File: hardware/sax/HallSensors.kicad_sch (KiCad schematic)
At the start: 2 parts, among them J1301 2x05_Horizontal

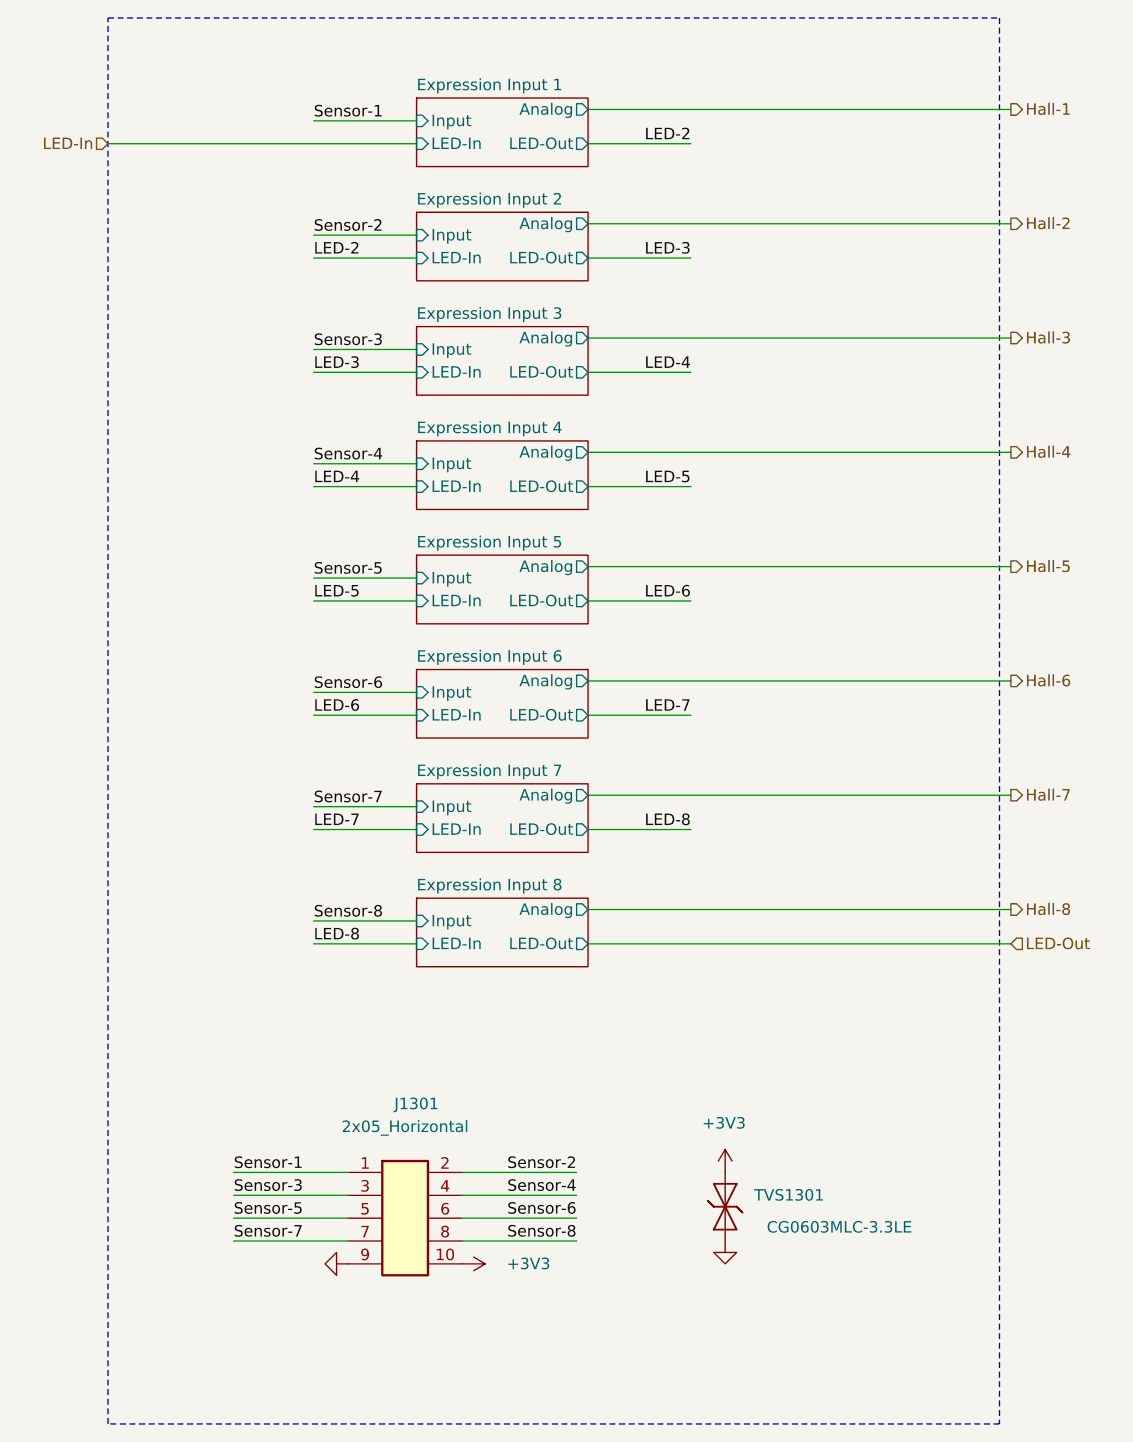
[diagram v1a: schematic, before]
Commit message: KiCad 10
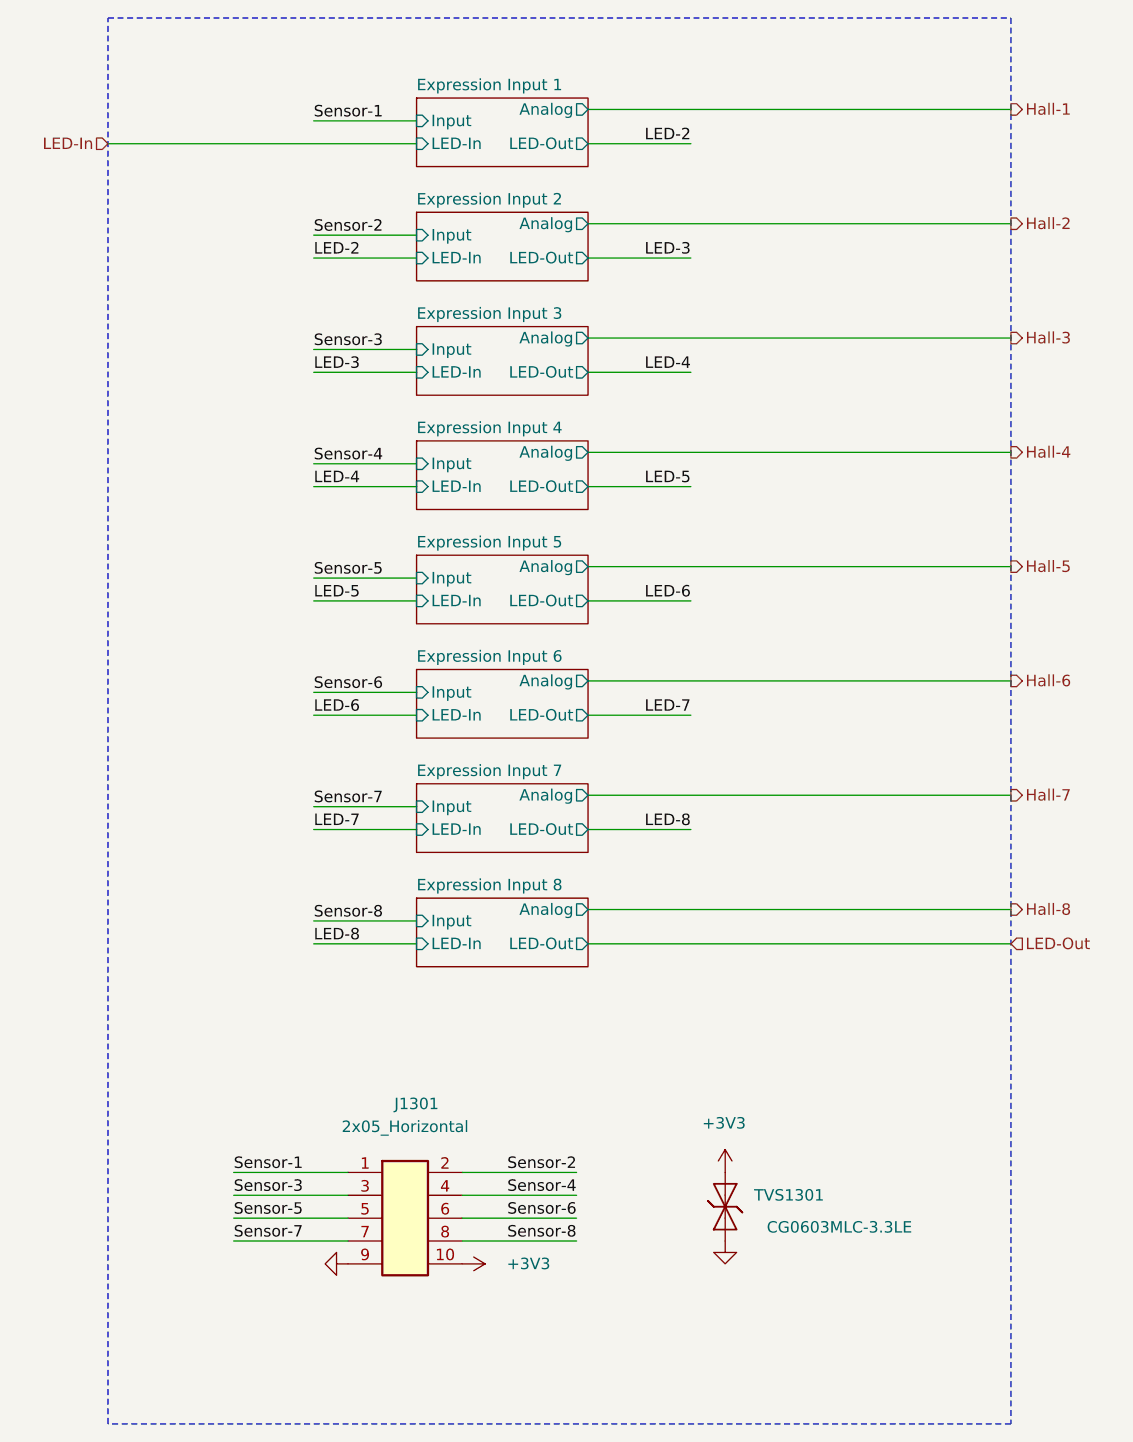
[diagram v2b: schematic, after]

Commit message: Replace step-down
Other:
- title: Hall Sensors -> V2 sax
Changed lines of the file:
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@@
 	(paper "A4")
 	(title_block
-		(title "Hall Sensors")
-		(date "2026-03-21")
-		(rev "2026-02-10")
+		(title "V2 sax")
+		(date "2026-03-31")
+		(rev "2026-03-31")
 		(company "Versio Duo")
 	)

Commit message: Limit up note length to 3 seconds
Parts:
- J1301: Id (none) -> Header:${SYMBOL_NAME}
- TVS1301: Id (none) -> Diode:${SYMBOL_NAME}
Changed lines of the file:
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@@
+			)
+		)
+		(property "Id" "Header:${SYMBOL_NAME}"
+			(at 132.08 172.72 0)
+			(hide yes)
+			(show_name no)
+			(do_not_autoplace no)
+			(effects
+				(font
+					(size 1.27 1.27)
+				)
+			)
+		)
+		(property "Sim.Enable" ""
+			(at 132.08 157.48 0)
+			(hide yes)
+			(show_name no)
+			(do_not_autoplace no)
+			(effects
+				(font
+					(size 1.27 1.27)
+				)
+			)
+		)
+		(property "Voltage" ""
+			(at 132.08 157.48 0)
+			(hide yes)
+			(show_name no)
+			(do_not_autoplace no)
+			(effects
+				(font
+					(size 1.27 1.27)
+				)
 			)
 		)
@@
 			(hide yes)
 			(show_name no)
+			(do_not_autoplace no)
+			(effects
+				(font
+					(size 1.27 1.27)
+				)
+			)
+		)
+		(property "Id" "Diode:${SYMBOL_NAME}"
+			(at 173.99 156.21 0)
+			(hide yes)
+			(show_name no)
+			(do_not_autoplace no)
+			(effects
+				(font
+					(size 1.27 1.27)
+				)
+			)
+		)
+		(property "Sim.Enable" ""
+			(at 167.64 156.21 90)
+			(hide yes)
+			(show_name no)
+			(do_not_autoplace no)
+			(effects
+				(font
+					(size 1.27 1.27)
+				)
+			)
+		)
+		(property "Voltage" ""
+			(at 167.64 156.21 90)
+			(hide yes)
+			(show_name no)
